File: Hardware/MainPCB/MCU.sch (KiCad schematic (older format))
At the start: 3 parts, among them U4 TPS22919

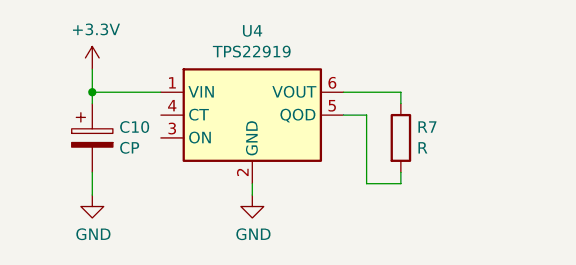
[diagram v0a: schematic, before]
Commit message: Discrete componenten rond IC's en IC's zelfs nagegaan. + toevoeging BOM
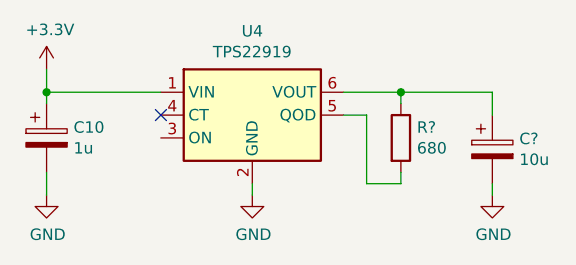
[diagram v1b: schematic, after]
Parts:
- added C?: 10u, symbol Device:CP
- C10: value CP -> 1u
- R?: renamed from R7; value R -> 680
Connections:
- net GND: now also C?.2
- net at R?.1, U4.6 (VOUT): now also C?.1
- no-connect marks 0 -> 1
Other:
- moved on the sheet: C10
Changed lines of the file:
@@
 	5450 4350 5450 4300
 $Comp
-L Device:R R7
+L Device:R R?
 U 1 1 5E608101
 P 6100 4100
-F 0 "R7" H 6170 4146 50  0000 L CNN
-F 1 "R" H 6170 4055 50  0000 L CNN
+F 0 "R?" H 6170 4146 50  0000 L CNN
+F 1 "680" H 6170 4055 50  0000 L CNN
 F 2 "" V 6030 4100 50  0001 C CNN
 F 3 "~" H 6100 4100 50  0001 C CNN
@@
 L power:+3.3V #PWR?
 U 1 1 5E60BCC8
-P 4750 3800
+P 4550 3800
 AR Path="/5E60BCC8" Ref="#PWR?"  Part="1"
 AR Path="/5E6059B5/5E60BCC8" Ref="#PWR029"  Part="1"
-F 0 "#PWR029" H 4750 3650 50  0001 C CNN
-F 1 "+3.3V" H 4765 3973 50  0000 C CNN
-F 2 "" H 4750 3800 50  0001 C CNN
-F 3 "" H 4750 3800 50  0001 C CNN
-	1    4750 3800
+F 0 "#PWR029" H 4550 3650 50  0001 C CNN
+F 1 "+3.3V" H 4565 3973 50  0000 C CNN
+F 2 "" H 4550 3800 50  0001 C CNN
+F 3 "" H 4550 3800 50  0001 C CNN
+	1    4550 3800
 	1    0    0    -1
 $EndComp
 Wire Wire Line
-	4750 3800 4750 3900
+	4550 3800 4550 3900
 $Comp
 L Device:CP C10
 U 1 1 5E60C590
-P 4750 4100
-F 0 "C10" H 4868 4146 50  0000 L CNN
-F 1 "CP" H 4868 4055 50  0000 L CNN
-F 2 "" H 4788 3950 50  0001 C CNN
-F 3 "~" H 4750 4100 50  0001 C CNN
-	1    4750 4100
+P 4550 4100
+F 0 "C10" H 4668 4146 50  0000 L CNN
+F 1 "1u" H 4668 4055 50  0000 L CNN
+F 2 "" H 4588 3950 50  0001 C CNN
+F 3 "~" H 4550 4100 50  0001 C CNN
+	1    4550 4100
 	1    0    0    -1
 $EndComp
@@
 L power:GND #PWR030
 U 1 1 5E60D5F3
-P 4750 4350
-F 0 "#PWR030" H 4750 4100 50  0001 C CNN
-F 1 "GND" H 4755 4177 50  0000 C CNN
-F 2 "" H 4750 4350 50  0001 C CNN
-F 3 "" H 4750 4350 50  0001 C CNN
-	1    4750 4350
+P 4550 4350
+F 0 "#PWR030" H 4550 4100 50  0001 C CNN
+F 1 "GND" H 4555 4177 50  0000 C CNN
+F 2 "" H 4550 4350 50  0001 C CNN
+F 3 "" H 4550 4350 50  0001 C CNN
+	1    4550 4350
 	1    0    0    -1
 $EndComp
 Wire Wire Line
-	4750 4350 4750 4250
+	4550 4350 4550 4250
 Wire Wire Line
-	4750 3950 4750 3900
-Connection ~ 4750 3900
+	4550 3950 4550 3900
+Connection ~ 4550 3900
+$Comp
+L Device:CP C?
+U 1 1 5E6BFE15
+P 6500 4150
+F 0 "C?" H 6618 4196 50  0000 L CNN
+F 1 "10u" H 6618 4105 50  0000 L CNN
+F 2 "" H 6538 4000 50  0001 C CNN
+F 3 "~" H 6500 4150 50  0001 C CNN
+	1    6500 4150
+	1    0    0    -1
+$EndComp
+$Comp
+L power:GND #PWR?
+U 1 1 5E6C0589
+P 6500 4350
+F 0 "#PWR?" H 6500 4100 50  0001 C CNN
+F 1 "GND" H 6505 4177 50  0000 C CNN
+F 2 "" H 6500 4350 50  0001 C CNN
+F 3 "" H 6500 4350 50  0001 C CNN
+	1    6500 4350
+	1    0    0    -1
+$EndComp
 Wire Wire Line
-	4750 3900 5050 3900
+	6500 4350 6500 4300
+Wire Wire Line
+	6100 3900 6500 3900
+Wire Wire Line
+	6500 3900 6500 4000
+Connection ~ 6100 3900
+Wire Wire Line
+	4550 3900 5050 3900
+NoConn ~ 5050 4000
 $EndSCHEMATC

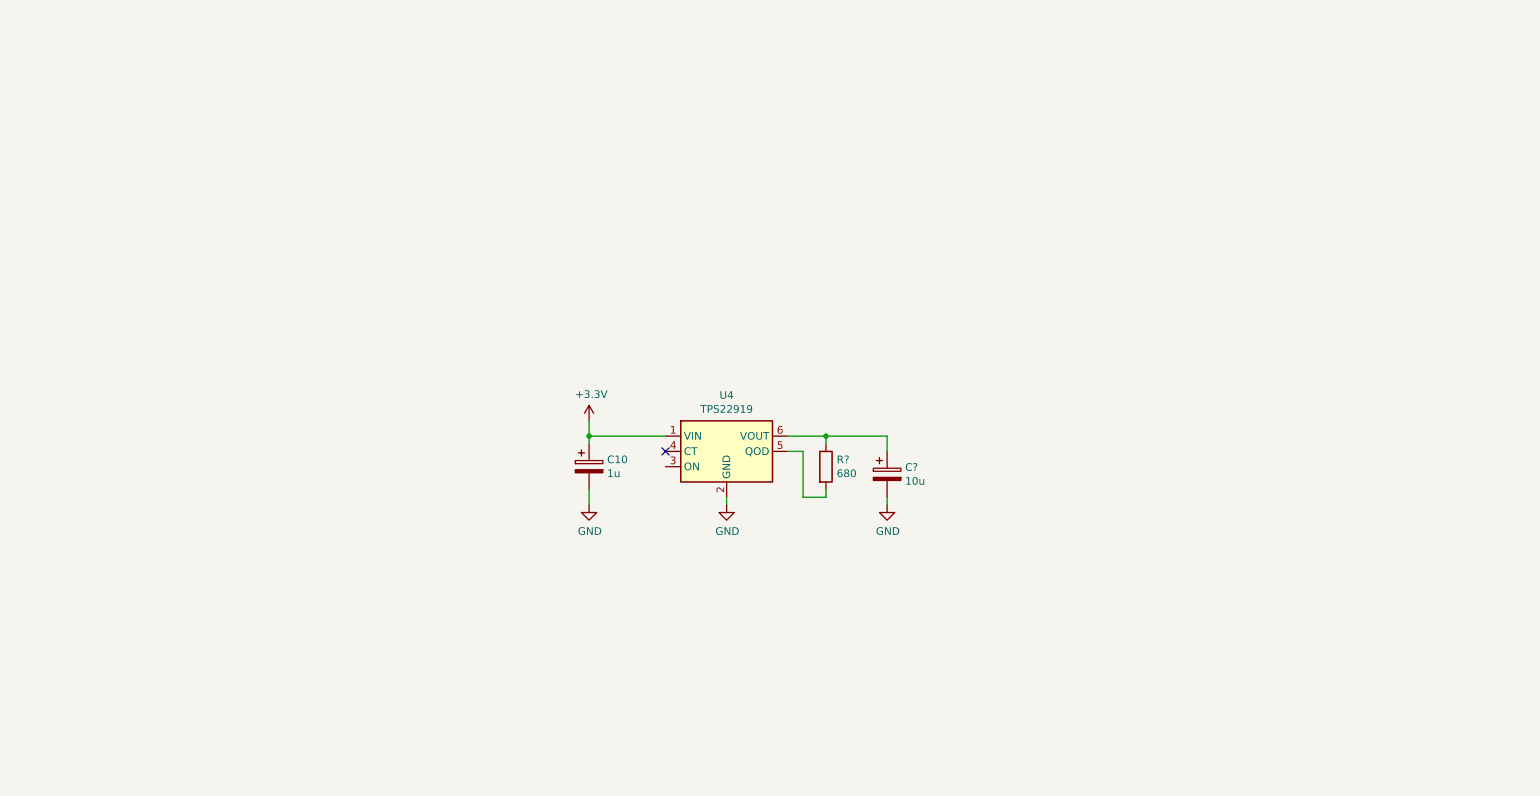
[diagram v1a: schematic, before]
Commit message: schematic voor esp32 mainboard
de esp toegevoegd en de nodige connecties gemaakt
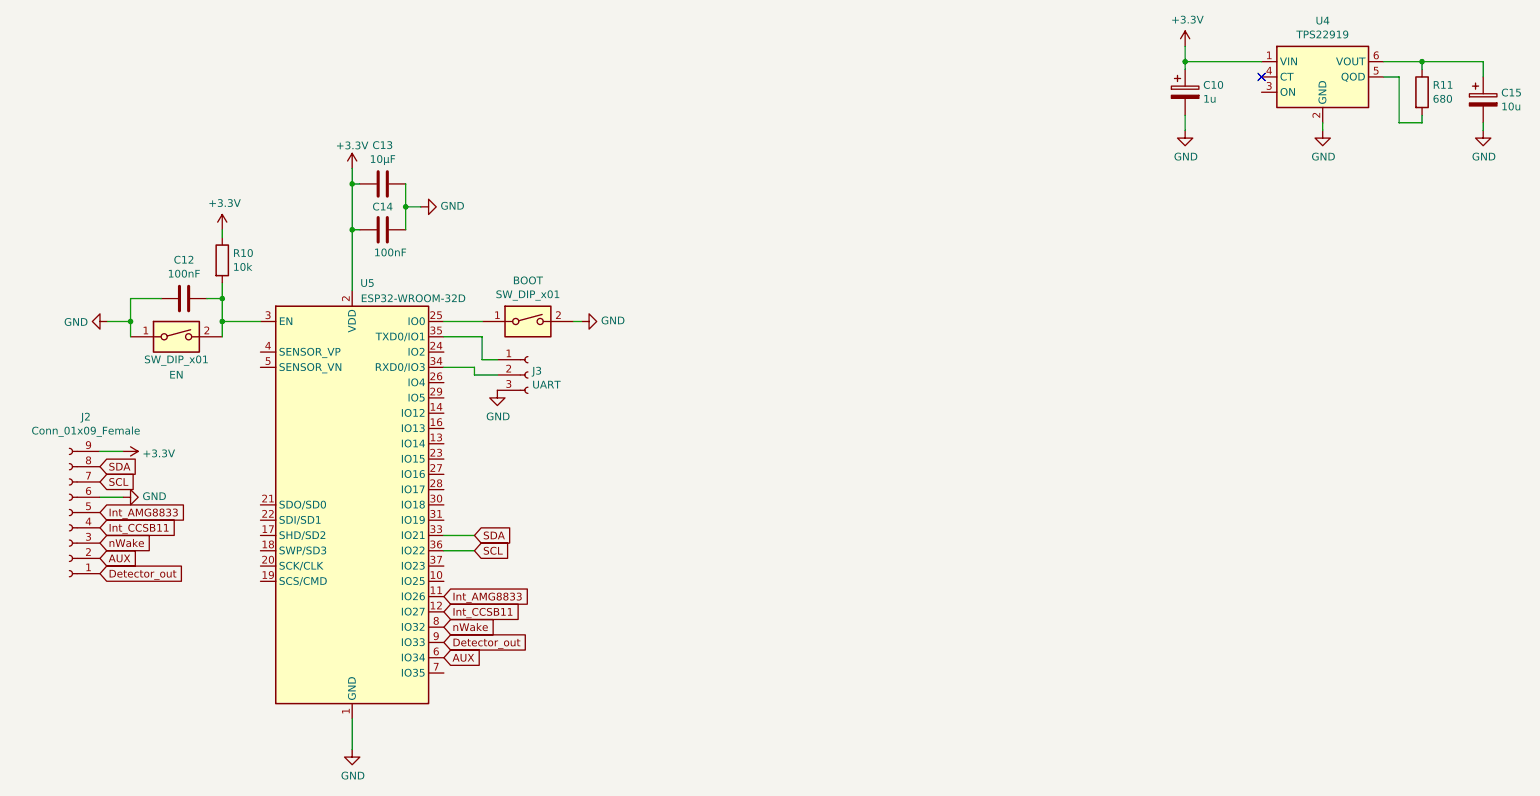
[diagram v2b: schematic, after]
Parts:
- added BOOT, EN: SW_DIP_x01, Button_Switch_SMD:SW_Push_1P1T_NO_6x6mm_H9.5mm, symbol Switch:SW_DIP_x01
- added C12, C14: 100nF, Capacitor_SMD:C_0805_2012Metric_Pad1.15x1.40mm_HandSolder, symbol Device:C
- added C13: 10µF, Capacitor_SMD:C_0805_2012Metric_Pad1.15x1.40mm_HandSolder, symbol Device:C
- added J2: Conn_01x09_Female, Connector_PinHeader_2.54mm:PinHeader_1x09_P2.54mm_Vertical, symbol Connector:Conn_01x09_Female
- added J3: UART, Connector_PinHeader_2.54mm:PinHeader_1x03_P2.54mm_Vertical, symbol Connector:Conn_01x03_Female
- added R10: 10k, Resistor_SMD:R_0805_2012Metric_Pad1.15x1.40mm_HandSolder, symbol Device:R
- added U5: ESP32-WROOM-32D, RF_Module:ESP32-WROOM-32, symbol RF_Module:ESP32-WROOM-32D
- gave numbers to parts that had none: 2
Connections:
- net +3V3: now also C13.2, C14.1, J2.9 (Pin_9), R10.1, U5.2 (VDD)
- net GND: now also BOOT.2, C12.2, C13.1, C14.2, EN.1, J2.6 (Pin_6), J3.3 (Pin_3), U5.1 (GND), U5.15 (GND), U5.38 (GND), U5.39 (GND)
- new net: BOOT.1, U5.25 (IO0)
- new net: C12.1, EN.2, R10.2, U5.3 (EN)
- new net: J3.2 (Pin_2), U5.34 (RXD0/IO3)
- new net: J3.1 (Pin_1), U5.35 (TXD0/IO1)
- new net AUX: J2.2 (Pin_2), U5.6 (IO34)
- new net Detector_out: J2.1 (Pin_1), U5.9 (IO33)
- new net Int_AMG8833: J2.5 (Pin_5), U5.11 (IO26)
- new net Int_CCSB11: J2.4 (Pin_4), U5.12 (IO27)
- new net SCL: J2.7 (Pin_7), U5.36 (IO22)
- new net SDA: J2.8 (Pin_8), U5.33 (IO21)
- new net nWake: J2.3 (Pin_3), U5.8 (IO32)
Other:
- moved on the sheet: C10, C15, R11, U4

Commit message: Main PCB volledig uitgerust met foorprints voor discrete componenten + BOM aangevuld met alles
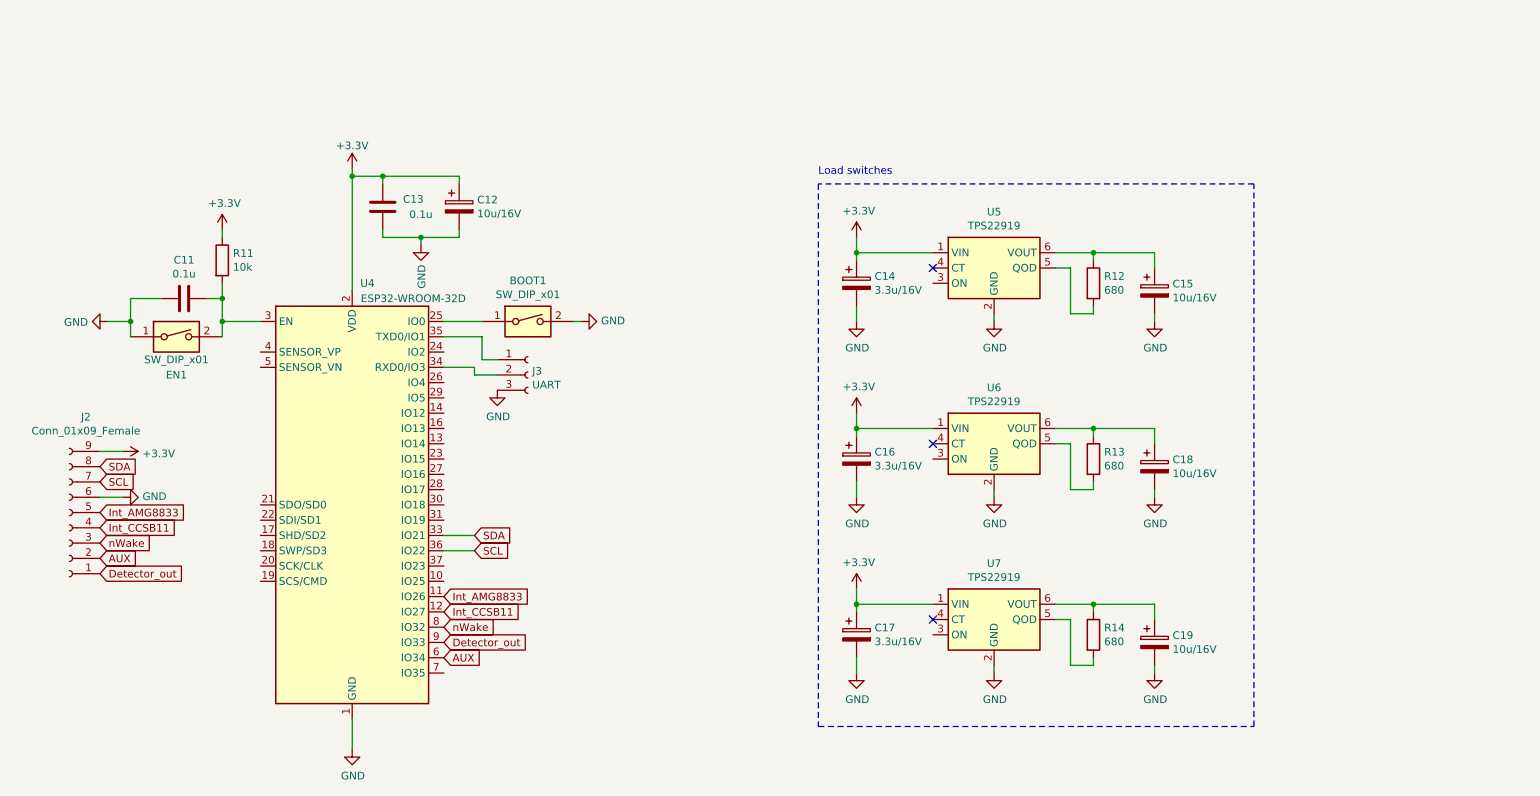
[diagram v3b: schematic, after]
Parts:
- removed C13: 10µF, Capacitor_SMD:C_0805_2012Metric_Pad1.15x1.40mm_HandSolder, symbol Device:C
- added C12, C18, C19: 10u/16V, Capacitor_SMD:CP_Elec_4x5.4, symbol Device:CP
- added C16, C17: 3.3u/16V, Capacitor_SMD:CP_Elec_4x5.4, symbol Device:CP
- added R13, R14: 680, Resistor_SMD:R_1206_3216Metric_Pad1.42x1.75mm_HandSolder, symbol Device:R
- added U6, U7: TPS22919, Package_TO_SOT_SMD:SOT-363_SC-70-6, symbol Power_Management:TPS22917DBV
- C11: renamed from C12; value 100nF -> 0.1u; footprint Capacitor_SMD:C_0805_2012Metric_Pad1.15x1.40mm_HandSolder -> Capacitor_SMD:C_1206_3216Metric_Pad1.42x1.75mm_HandSolder
- C13: renamed from C14; value 100nF -> 0.1u; footprint Capacitor_SMD:C_0805_2012Metric_Pad1.15x1.40mm_HandSolder -> Capacitor_SMD:C_1206_3216Metric_Pad1.42x1.75mm_HandSolder
- C14: renamed from C10; value 1u -> 3.3u/16V; footprint (none) -> Capacitor_SMD:CP_Elec_4x5.4
- C15: value 10u -> 10u/16V; footprint (none) -> Capacitor_SMD:CP_Elec_4x5.4
- R11: renamed from R10; footprint Resistor_SMD:R_0805_2012Metric_Pad1.15x1.40mm_HandSolder -> Resistor_SMD:R_1206_3216Metric_Pad1.42x1.75mm_HandSolder
- R12: renamed from R11; footprint (none) -> Resistor_SMD:R_1206_3216Metric_Pad1.42x1.75mm_HandSolder
- renumbered BOOT to BOOT1, EN to EN1, U5 to U4, U4 to U5
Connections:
- net +3V3: now also C13.2, C12.1, C16.1, C17.1, U6.1 (VIN), U7.1 (VIN); no longer C13.1
- net GND: now also C13.1, C12.2, C16.2, C17.2, C18.2, C19.2, U6.2 (GND), U7.2 (GND); no longer C13.2
- new net: R13.2, U6.5 (QOD)
- new net: C18.1, R13.1, U6.6 (VOUT)
- new net: R14.2, U7.5 (QOD)
- new net: C19.1, R14.1, U7.6 (VOUT)
- no-connect marks 1 -> 3
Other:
- note added: "Load switches"
- moved on the sheet: C13, C14, C15, R12, U5

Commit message: Eerste plaatsing van componenten op PCB
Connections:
- net PowerS1: now reaches U5.3 (ON)
- net PowerS1: now also U4.23 (IO15)
- net PowerS2: now reaches U4.27 (IO16)
- net PowerS2: now also U6.3 (ON)
- net PowerS3: now reaches U4.28 (IO17)
- net PowerS3: now also U7.3 (ON)
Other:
- note added: "Verplaats gerust als je deze GPIO pinnen zou nodig hebben.\n"
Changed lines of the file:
@@
 Text Notes 6050 2200 0    50   ~ 0
 Load switches
+Text GLabel 3850 4050 2    50   Input ~ 0
+PowerS1
+Text GLabel 3850 4150 2    50   Input ~ 0
+PowerS2
+Text GLabel 3850 4250 2    50   Input ~ 0
+PowerS3
+Wire Wire Line
+	3600 4250 3850 4250
+Wire Wire Line
+	3850 4150 3600 4150
+Wire Wire Line
+	3600 4050 3850 4050
+Text Notes 3850 4000 0    39   ~ 0
+Verplaats gerust als je deze GPIO pinnen zou nodig hebben.\n
+Text GLabel 6600 3050 3    50   Input ~ 0
+PowerS1
+Wire Wire Line
+	6600 3050 6600 2900
+Wire Wire Line
+	6600 2900 6800 2900
+Text GLabel 6600 4200 3    50   Input ~ 0
+PowerS2
+Wire Wire Line
+	6600 4200 6600 4050
+Wire Wire Line
+	6600 4050 6800 4050
+Text GLabel 6650 5350 3    50   Input ~ 0
+PowerS3
+Wire Wire Line
+	6650 5350 6650 5200
+Wire Wire Line
+	6650 5200 6800 5200
 $EndSCHEMATC

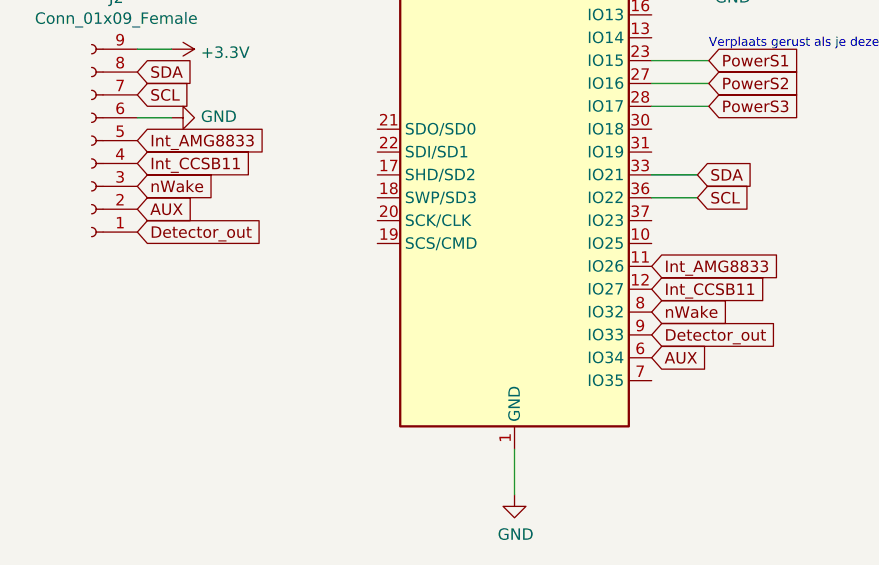
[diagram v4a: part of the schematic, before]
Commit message: Aux pin verwijderd + aanpassing gedaan VSS naar -VBAT en GND op de juiste plaats gezet
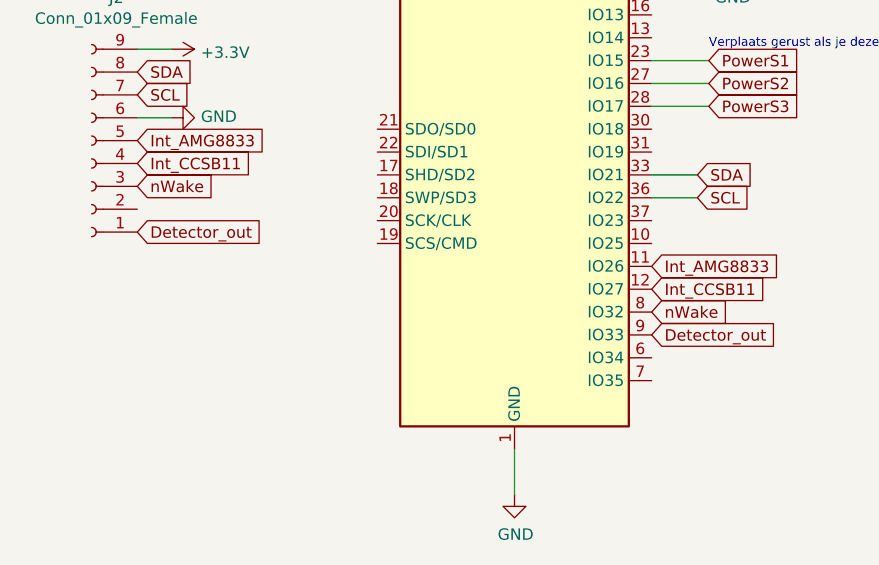
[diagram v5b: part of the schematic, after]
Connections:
- net AUX: no longer names the net of U4.6 (IO34)
- net AUX: no longer J2.2 (Pin_2)
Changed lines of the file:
@@
 Text GLabel 1350 4600 2    50   Input ~ 0
 nWake
-Text GLabel 1350 4700 2    50   Input ~ 0
-AUX
 Text GLabel 1350 4800 2    50   Input ~ 0
 Detector_out
@@
 Text GLabel 3600 5250 2    50   Input ~ 0
 Detector_out
-Text GLabel 3600 5350 2    50   Input ~ 0
-AUX
 $Comp
 L Device:CP C12
